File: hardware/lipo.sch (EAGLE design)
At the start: 50 parts, among them J1 MICRO_USB_B_HIROSE_ZX62-B-5PA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, Q1 IRLML6402, Q2 IRLML6344, SW1 TVAF06-A020B-R, U1 LT6106CS5#PBF, U2 NJM12888F, X1 FA-238

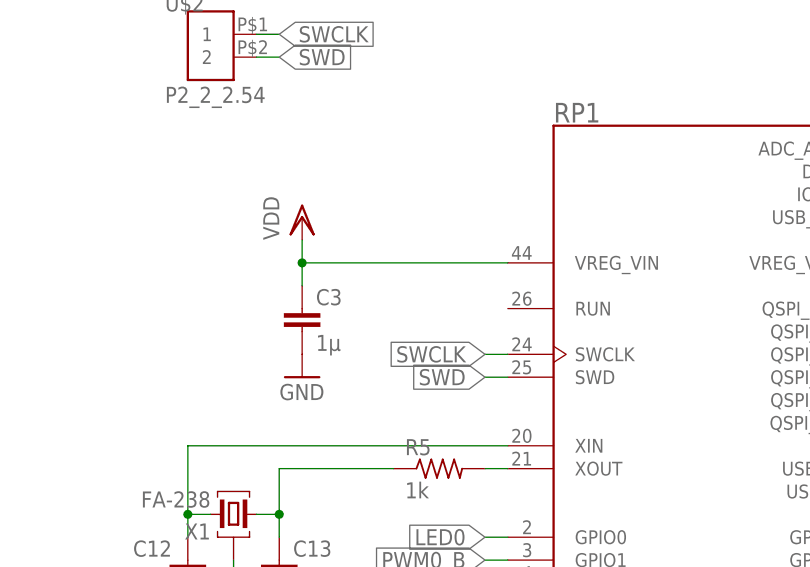
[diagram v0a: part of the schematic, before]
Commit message: べたGND前です。esp32のschはノータッチなのでここに上がってないです。よろしくお願いします。
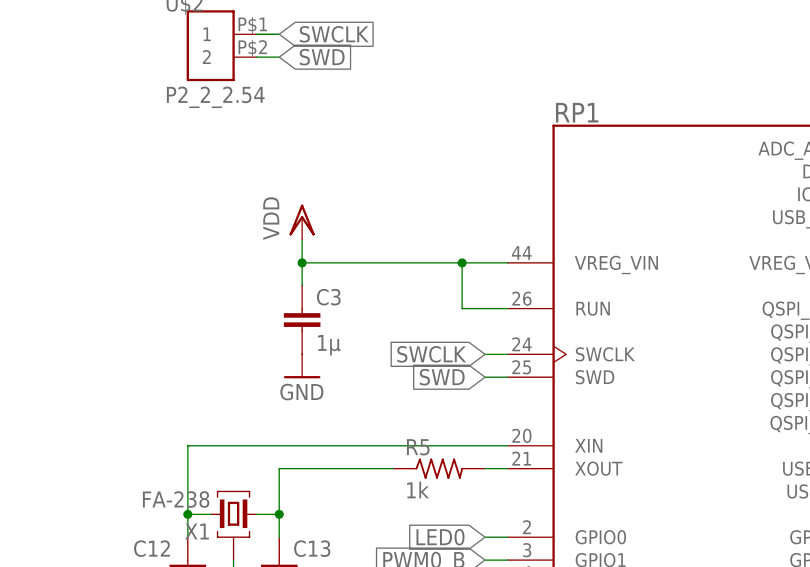
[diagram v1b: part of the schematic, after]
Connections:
- net VDD: now also RP1.RUN
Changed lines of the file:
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@@
 <segment>
 <pinref part="RP1" gate="G$1" pin="VREG_VIN"/>
-<wire x1="33.02" y1="127" x2="10.16" y2="127" width="0.1524" layer="91"/>
+<wire x1="33.02" y1="127" x2="27.94" y2="127" width="0.1524" layer="91"/>
 <pinref part="C3" gate="G$1" pin="1"/>
+<wire x1="27.94" y1="127" x2="10.16" y2="127" width="0.1524" layer="91"/>
 <wire x1="10.16" y1="127" x2="10.16" y2="124.46" width="0.1524" layer="91"/>
 <wire x1="10.16" y1="127" x2="10.16" y2="129.54" width="0.1524" layer="91"/>
 <junction x="10.16" y="127"/>
 <pinref part="VDD8" gate="G$1" pin="VDD"/>
+<pinref part="RP1" gate="G$1" pin="RUN"/>
+<wire x1="33.02" y1="121.92" x2="27.94" y2="121.92" width="0.1524" layer="91"/>
+<wire x1="27.94" y1="121.92" x2="27.94" y2="127" width="0.1524" layer="91"/>
+<junction x="27.94" y="127"/>
 </segment>
 </net>

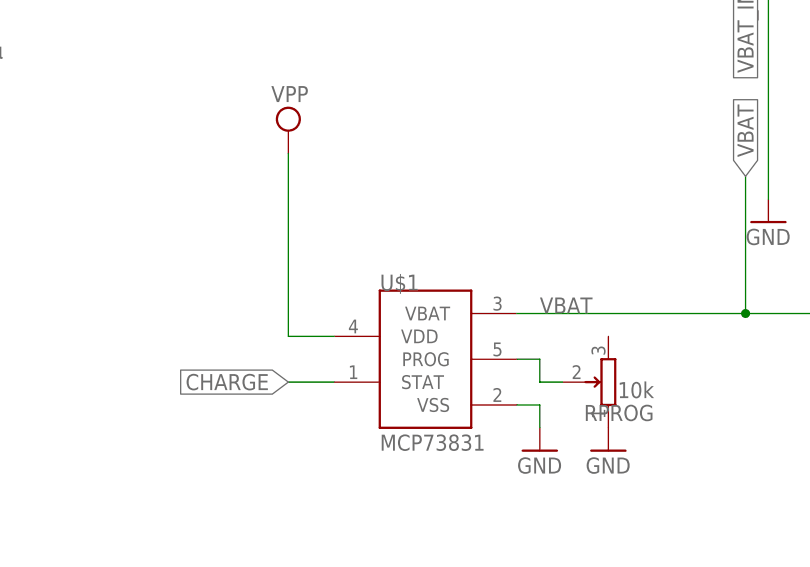
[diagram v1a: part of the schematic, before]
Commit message: シルクを調整
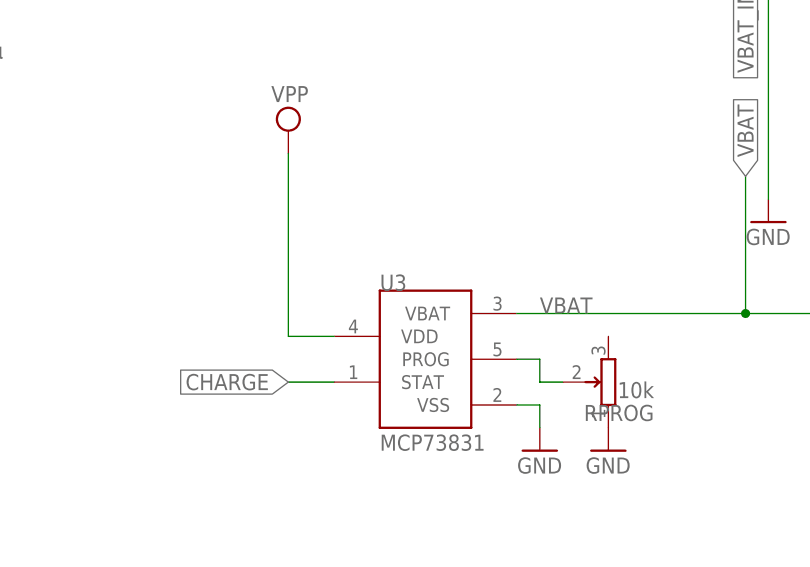
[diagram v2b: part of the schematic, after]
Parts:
- renumbered U$1 to U3
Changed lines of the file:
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@@
 <part name="U$2" library="pins" deviceset="P2_2_2.54" device=""/>
 <part name="BAT" library="jst-ph" deviceset="S2B-PH-*" device="K-S"/>
-<part name="U$1" library="mcp73831" deviceset="MCP73831" device=""/>
+<part name="U3" library="mcp73831" deviceset="MCP73831" device=""/>
 <part name="GND1" library="supply1" library_urn="urn:adsk.eagle:library:371" deviceset="GND" device=""/>
 <part name="HEATER" library="jst-ph" deviceset="S3B-PH-*" device="K-S"/>
@@
 <attribute name="VALUE" x="256.54" y="143.51" size="1.778" layer="96" rot="R90"/>
 </instance>
-<instance part="U$1" gate="G$1" x="213.36" y="96.52" smashed="yes">
+<instance part="U3" gate="G$1" x="213.36" y="96.52" smashed="yes">
 <attribute name="NAME" x="208.28" y="104.14" size="1.778" layer="95"/>
 <attribute name="VALUE" x="208.28" y="86.36" size="1.778" layer="96"/>
@@
 </segment>
 <segment>
-<pinref part="U$1" gate="G$1" pin="VSS"/>
+<pinref part="U3" gate="G$1" pin="VSS"/>
 <wire x1="223.52" y1="91.44" x2="226.06" y2="91.44" width="0.1524" layer="91"/>
 <wire x1="226.06" y1="91.44" x2="226.06" y2="88.9" width="0.1524" layer="91"/>
@@
 <net name="CHARGE" class="0">
 <segment>
-<pinref part="U$1" gate="G$1" pin="STAT"/>
+<pinref part="U3" gate="G$1" pin="STAT"/>
 <wire x1="203.2" y1="93.98" x2="198.12" y2="93.98" width="0.1524" layer="91"/>
 <label x="198.12" y="93.98" size="1.778" layer="95" rot="R180" xref="yes"/>
@@
 <net name="VBAT" class="0">
 <segment>
-<pinref part="U$1" gate="G$1" pin="VBAT"/>
+<pinref part="U3" gate="G$1" pin="VBAT"/>
 <wire x1="223.52" y1="101.6" x2="248.92" y2="101.6" width="0.1524" layer="91"/>
 <pinref part="Q1" gate="G$1" pin="D"/>
@@
 <wire x1="228.6" y1="93.98" x2="226.06" y2="93.98" width="0.1524" layer="91"/>
 <wire x1="226.06" y1="93.98" x2="226.06" y2="96.52" width="0.1524" layer="91"/>
-<pinref part="U$1" gate="G$1" pin="PROG"/>
+<pinref part="U3" gate="G$1" pin="PROG"/>
 <wire x1="226.06" y1="96.52" x2="223.52" y2="96.52" width="0.1524" layer="91"/>
 </segment>
@@
 </segment>
 <segment>
-<pinref part="U$1" gate="G$1" pin="VDD"/>
+<pinref part="U3" gate="G$1" pin="VDD"/>
 <wire x1="203.2" y1="99.06" x2="198.12" y2="99.06" width="0.1524" layer="91"/>
 <wire x1="198.12" y1="99.06" x2="198.12" y2="119.38" width="0.1524" layer="91"/>

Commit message: 若干修正
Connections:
- removed net N$7: U1.V-
- net GND: now also U1.V-
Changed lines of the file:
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@@
 <pinref part="GND11" gate="1" pin="GND"/>
+</segment>
+<segment>
+<pinref part="U1" gate="G$1" pin="V-"/>
+<wire x1="325.12" y1="78.74" x2="322.58" y2="78.74" width="0.1524" layer="91"/>
+<pinref part="GND6" gate="1" pin="GND"/>
+<wire x1="322.58" y1="78.74" x2="322.58" y2="71.12" width="0.1524" layer="91"/>
 </segment>
 </net>
@@
 </segment>
 </net>
-<net name="N$7" class="0">
-<segment>
-<pinref part="U1" gate="G$1" pin="V-"/>
-<wire x1="325.12" y1="78.74" x2="322.58" y2="78.74" width="0.1524" layer="91"/>
-<wire x1="322.58" y1="78.74" x2="322.58" y2="71.12" width="0.1524" layer="91"/>
-<pinref part="GND6" gate="1" pin="GND"/>
-</segment>
-</net>

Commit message: LiPo回路修正，新LoRa
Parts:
- removed D1, D2: CUHS20S30, diodes:CUHS20S30
- removed Q2: IRLML6344, mosfet:IRLML6344
- added C15: 10µF, rcl:C-EUC0402
- added C18: 0.1µF, rcl:C-EUC0402
- added L1: 4.7µH, rcl:L-USL3225M
- added R14: 100k, rcl:R-US_R0402
- added R15: 100, rcl:R-US_R0402
- added S1: SSAJ120100, SSAJ120100:SSAJ120100
- added U$1: TPS63000, TPS63000:TPS63000
- added U$3: S2B-ZR, con-jst-zh:S2B-ZR
- added U5: TCK106AF,LF, TCK106AF_LF:TCK106AF,LF
- added VR1: 22k, potentiometers:PVZ3A
- C16: value (none) -> 10µF; device rcl:CPOL-EU153CLV-0605 -> rcl:C-EUC0402
- R13: value 22k -> 10k
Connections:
- net ISENSE renamed V+_I
- net VSENSE renamed BAT_V
- removed net N$10: HEATER.3, Q2.D
- removed net N$6: D1.A, J1.+5V
- removed net V: C16.+, D3.C, Q1.S, R11.2, R8.1, R9.2, U1.V+
- removed net VBAT_IN: BAT.1
- removed net VSUP: D2.A
- removed net VSUP_IN: SUPPLY.1
- new net EN: C18.1, S1.2, U$1.EN, U$1.PS/SYNC, U$1.VINA, U$3G$2.1
- new net N$1: L1.1, U$1.L1
- new net N$13: HEATER.1, U5.VOUT
- new net N$14: R15.2, S1.C, U$3G$1.1
- new net N$3: C15.1, D3.C, Q1.S, R15.1, U$1.VIN, U5.VIN
- new net N$7: L1.2, U$1.L2
- new net SUPPLY_V: R14.2, R7.1
- new net V+_V: U$1.FB, VR1.2
- new net VOUT: C16.1, R8.1, R9.2, U$1.VOUT, U1.V+, VR1.1
- net GND: now also C15.2, C16.2, C18.2, HEATER.2, R14.1, U$1.GND, U$1.PG, U$1.PGND, U5.GND, VR1.3; no longer C16.-, Q2.S, R13.1, R7.1
- net HEATER: now also U5.CONTROL; no longer Q2.G
- net TEMP: now also HEATER.3, R13.1; no longer HEATER.2, R13.2
- net V+: no longer HEATER.1
- net VBAT: now also BAT.1, R11.2
- net VDD: now also R13.2
- net VPP: now also J1.+5V, SUPPLY.1; no longer D1.C, D2.C
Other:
- moved on the sheet: BAT, HEATER, R10, R11, R12, R13, R8, R9, SUPPLY, U1

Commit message: アナログ入力を修正
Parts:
- added IC1, IC2: 4066D, 40xx:4066D
- added NTC: 10k, rcl:R-EU_R0603
- added R16: 0.033, rcl:R-US_R0603
- added R17: 10k, rcl:R-US_R0402
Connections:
- removed net ADC3: RP1.GPIO29/ADC3
- removed net I2C0_SDA: RP1.GPIO8
- removed net I2C1_SCL: RP1.GPIO7
- removed net I2C1_SDA: RP1.GPIO6
- removed net I2C_SCL: RP1.GPIO9
- removed net PWM0_B: RP1.GPIO1
- removed net PWM1_A: RP1.GPIO2
- removed net PWM1_B: RP1.GPIO3
- removed net PWM3_A: RP1.GPIO22
- removed net PWM4_A: RP1.GPIO24
- removed net PWM5_A: RP1.GPIO10
- removed net PWM5_B: RP1.GPIO11
- removed net SPI0_CS: RP1.GPIO21
- removed net SPI0_MISO: RP1.GPIO20
- removed net SPI0_MOSI: RP1.GPIO19
- removed net SPI0_SCK: RP1.GPIO18
- removed net SPI1_CS: RP1.GPIO13
- removed net SPI1_MISO: RP1.GPIO12
- removed net SPI1_MOSI: RP1.GPIO15
- removed net SPI1_SCK: RP1.GPIO14
- new net ADC0_IN: IC1A.B, IC1B.B, RP1.GPIO26/ADC0
- new net ADC1_IN: IC1C.B, IC1D.B, RP1.GPIO27/ADC1
- new net ADC2_IN: IC2A.B, IC2B.B, IC2C.B, RP1.GPIO28/ADC2
- new net ADC_SEL1: IC1A.C, IC1C.C, IC2A.C
- new net ADC_SEL2: IC1B.C, IC1D.C, IC2B.C
- new net ADC_SEL3: IC2C.C
- new net HEATER_I: HEATER.2, IC1D.A, R16.2
- new net OB_TEMP: IC2C.A, NTC.2, R17.1
- net BAT_V: now also IC1B.A; no longer RP1.GPIO27/ADC1
- net GND: now also NTC.1, R16.1; no longer HEATER.2
- net SUPPLY_V: now also IC1A.A
- net TEMP: now also IC2B.A; no longer RP1.GPIO28/ADC2
- net V+_I: now also IC1C.A; no longer RP1.GPIO26/ADC0
- net V+_V: now also IC2A.A
- net VDD: now also R17.2
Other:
- moved on the sheet: HEATER, R13

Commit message: 回路微修正
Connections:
- removed net N$5: J1.ID
- net ADC_SEL1: now also RP1.GPIO13
- net ADC_SEL2: now also RP1.GPIO20
- net ADC_SEL3: now also RP1.GPIO18
- net CHARGE: now also RP1.GPIO15
- net GND: now also IC1P.VSS, IC2P.VSS
- net HEATER: now also RP1.GPIO14
- net VDD: now also IC1P.VDD, IC2P.VDD
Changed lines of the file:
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@@
 <part name="R17" library="rcl" library_urn="urn:adsk.eagle:library:334" deviceset="R-US_" device="R0402" package3d_urn="urn:adsk.eagle:package:23547/3" value="10k"/>
 <part name="R16" library="rcl" library_urn="urn:adsk.eagle:library:334" deviceset="R-US_" device="R0603" package3d_urn="urn:adsk.eagle:package:23555/3" value="0.033"/>
+<part name="VDD3" library="supply1" library_urn="urn:adsk.eagle:library:371" deviceset="VDD" device=""/>
+<part name="VDD4" library="supply1" library_urn="urn:adsk.eagle:library:371" deviceset="VDD" device=""/>
+<part name="GND17" library="supply1" library_urn="urn:adsk.eagle:library:371" deviceset="GND" device=""/>
+<part name="GND18" library="supply1" library_urn="urn:adsk.eagle:library:371" deviceset="GND" device=""/>
 </parts>
 <sheets>
@@
 <attribute name="VALUE" x="344.17" y="42.418" size="1.778" layer="96"/>
 </instance>
+<instance part="IC1" gate="P" x="287.02" y="-2.54" smashed="yes">
+<attribute name="NAME" x="285.75" y="-3.175" size="1.778" layer="95"/>
+</instance>
+<instance part="IC2" gate="P" x="287.02" y="-71.12" smashed="yes">
+<attribute name="NAME" x="285.75" y="-71.755" size="1.778" layer="95"/>
+</instance>
+<instance part="VDD3" gate="G$1" x="287.02" y="-60.96" smashed="yes">
+<attribute name="VALUE" x="284.48" y="-63.5" size="1.778" layer="96" rot="R90"/>
+</instance>
+<instance part="VDD4" gate="G$1" x="287.02" y="7.62" smashed="yes">
+<attribute name="VALUE" x="284.48" y="5.08" size="1.778" layer="96" rot="R90"/>
+</instance>
+<instance part="GND17" gate="1" x="287.02" y="-12.7" smashed="yes">
+<attribute name="VALUE" x="284.48" y="-15.24" size="1.778" layer="96"/>
+</instance>
+<instance part="GND18" gate="1" x="287.02" y="-81.28" smashed="yes">
+<attribute name="VALUE" x="284.48" y="-83.82" size="1.778" layer="96"/>
+</instance>
 </instances>
 <busses>
@@
 <label x="93.98" y="101.6" size="1.778" layer="95" xref="yes"/>
 <pinref part="R2" gate="G$1" pin="2"/>
-</segment>
-</net>
-<net name="N$5" class="0">
-<segment>
-<pinref part="J1" gate="G$1" pin="ID"/>
-<wire x1="20.32" y1="172.72" x2="22.86" y2="172.72" width="0.1524" layer="91"/>
 </segment>
 </net>
@@
 <pinref part="NTC" gate="G$1" pin="1"/>
 <pinref part="GND8" gate="1" pin="GND"/>
+</segment>
+<segment>
+<pinref part="IC1" gate="P" pin="VSS"/>
+<pinref part="GND17" gate="1" pin="GND"/>
+</segment>
+<segment>
+<pinref part="IC2" gate="P" pin="VSS"/>
+<pinref part="GND18" gate="1" pin="GND"/>
 </segment>
 </net>
@@
 <pinref part="VDD2" gate="G$1" pin="VDD"/>
 </segment>
+<segment>
+<pinref part="IC2" gate="P" pin="VDD"/>
+<pinref part="VDD3" gate="G$1" pin="VDD"/>
+</segment>
+<segment>
+<pinref part="IC1" gate="P" pin="VDD"/>
+<pinref part="VDD4" gate="G$1" pin="VDD"/>
+</segment>
 </net>
 <net name="USB_DM_1" class="0">
@@
 <label x="198.12" y="93.98" size="1.778" layer="95" rot="R180" xref="yes"/>
 </segment>
+<segment>
+<pinref part="RP1" gate="G$1" pin="GPIO15"/>
+<wire x1="78.74" y1="96.52" x2="81.28" y2="96.52" width="0.1524" layer="91"/>
+<label x="81.28" y="96.52" size="1.778" layer="95" xref="yes"/>
+</segment>
 </net>
 <net name="N$4" class="0">
@@
 <wire x1="299.72" y1="45.72" x2="292.1" y2="45.72" width="0.1524" layer="91"/>
 <pinref part="U5" gate="G$1" pin="CONTROL"/>
+</segment>
+<segment>
+<pinref part="RP1" gate="G$1" pin="GPIO14"/>
+<wire x1="33.02" y1="60.96" x2="30.48" y2="60.96" width="0.1524" layer="91"/>
+<label x="30.48" y="60.96" size="1.778" layer="95" rot="R180" xref="yes"/>
 </segment>
 </net>
@@
 </segment>
 </net>
-<net name="VOUT1" class="0">
-<segment>
-<wire x1="403.86" y1="101.6" x2="447.04" y2="101.6" width="0.1524" layer="91"/>
-</segment>
-</net>
 <net name="VBAT" class="0">
 <segment>
@@
 <label x="215.9" y="22.86" size="1.778" layer="95" rot="R90" xref="yes"/>
 </segment>
+<segment>
+<pinref part="RP1" gate="G$1" pin="GPIO13"/>
+<wire x1="33.02" y1="63.5" x2="30.48" y2="63.5" width="0.1524" layer="91"/>
+<label x="30.48" y="63.5" size="1.778" layer="95" rot="R180" xref="yes"/>
+</segment>
 </net>
 <net name="ADC_SEL2" class="0">
@@
 <label x="213.36" y="22.86" size="1.778" layer="95" rot="R90" xref="yes"/>
 </segment>
+<segment>
+<pinref part="RP1" gate="G$1" pin="GPIO20"/>
+<wire x1="78.74" y1="83.82" x2="81.28" y2="83.82" width="0.1524" layer="91"/>
+<label x="81.28" y="83.82" size="1.778" layer="95" xref="yes"/>
+</segment>
 </net>
 <net name="ADC_SEL3" class="0">
@@
 <label x="210.82" y="22.86" size="1.778" layer="95" rot="R90" xref="yes"/>
 </segment>
-</net>
+<segment>
+<pinref part="RP1" gate="G$1" pin="GPIO18"/>
+<wire x1="78.74" y1="88.9" x2="81.28" y2="88.9" width="0.1524" layer="91"/>
+<label x="81.28" y="88.9" size="1.778" layer="95" xref="yes"/>
+</segment>
+</net>

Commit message: ベタ・シルク調整
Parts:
- renumbered RPROG to VRP, U$1 to U4, U$3 to SW
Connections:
- net N$13 renamed HEATER_OUT
- net N$3 renamed VBAT_
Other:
- moved on the sheet: HEATER, R13
